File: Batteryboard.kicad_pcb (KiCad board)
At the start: 4 copper layers, 75.8 x 76.2 mm, 143 parts, among them IC1 FAN4010IL6X_F113, IC2 FAN4010IL6X_F113, IC3 FAN4010IL6X_F113, J1 Conn_01x02_Male, J2 Conn_01x03_Male, J4 Conn_01x02_Male, J5 SC_19-20, Q1 SI7617DN-T1-GE3, Q2 SI7617DN-T1-GE3, Q3 SI7617DN-T1-GE3, Q4 SIS412DN-T1-GE3, Q5 SIS412DN-T1-GE3, Q6 SIS412DN-T1-GE3, Q7 SI7617DN-T1-GE3, Q8 SIS412DN-T1-GE3, U1 BQ24617RGET, U2 TPS65279DAPR, U3 BQ29200DRBT, U4 PIC18F25K50-I_SO, U5 MCP2515-xSO, U6 SN65HVD1050D

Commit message: added layout for buck converter
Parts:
- CTTC1: value 43nF -> 47nF
- moved TMP1 64.3 mm to (224.6, 77.6), turned to 270 degrees
- moved R41 39.3 mm to (216.7, 90.6)
- moved R43 34.5 mm to (222.4, 81.9), turned to 180 degrees
- moved C47 33.4 mm to (224.5, 73.1), turned to 270 degrees
- moved C31 30.6 mm to (222.1, 73.0), turned to 270 degrees
- moved C18 30.1 mm to (231.5, 73.0), turned to 270 degrees
- moved IC2 29.0 mm to (216.7, 88.2), turned to 270 degrees
- moved C48 28.5 mm to (226.8, 73.0), turned to 270 degrees
- moved R25 25.1 mm to (237.5, 94.2), turned to 90 degrees
- moved L3 24.6 mm to (242.5, 72.7), turned to 90 degrees
- moved C19 23.1 mm to (231.5, 69.6), turned to 90 degrees
- moved R24 23.1 mm to (233.0, 76.4), turned to 270 degrees
- moved C27 22.7 mm to (248.1, 88.4), turned to 180 degrees
- moved R23 22.3 mm to (231.1, 76.4), turned to 270 degrees
- moved R30 21.8 mm to (237.6, 69.6), turned to 270 degrees
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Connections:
- C1 pad 1: Q5S -> PGND2
- C10 pad 2: Q5S -> PGND2
- C12 pad 2: Q5S -> PGND2
- C13 pad 2: Q5S -> PGND2
- C16 pad 2: Q5S -> PGND2
- C19 pad 2: Q5S -> PGND2
- C2 pad 2: Q5S -> PGND2
- C20 pad 2: Q5S -> PGND2
- C21 pad 2: Q5S -> PGND2
- C22 pad 2: Q5S -> PGND2
- C23 pad 1: Q5S -> PGND2
- C26 pad 1: Q5S -> PGND2
- C27 pad 1: Q5S -> PGND2
- C28 pad 1: Q5S -> PGND2
- C29 pad 1: Q5S -> PGND2
- C31 pad 1: Q5S -> PGND2
- C32 pad 2: Q5S -> PGND2
- C33 pad 1: Q5S -> PGND2
- C34 pad 1: Q5S -> PGND2
- C35 pad 2: Q5S -> PGND2
- C36 pad 2: Q5S -> PGND2
- C37 pad 1: Q5S -> PGND2
- C38 pad 2: Q5S -> PGND2
- C39 pad 1: Q5S -> PGND2
- C4 pad 2: Q5S -> PGND2
- C40 pad 2: Q5S -> PGND2
- C41 pad 1: Q5S -> PGND2
- C42 pad 1: Q5S -> PGND2
- C43 pad 2: Q5S -> PGND2
- C44 pad 1: Q5S -> PGND2
- C45 pad 1: Q5S -> PGND2
- C46 pad 1: Q5S -> PGND2
- C47 pad 1: Q5S -> PGND2
- C48 pad 1: Q5S -> PGND2
- C49 pad 1: Q5S -> PGND2
- C5 pad 2: Q5S -> PGND2
- C7 pad 2: Q5S -> PGND2
- C8 pad 2: Q5S -> PGND2
- C9 pad 2: Q5S -> PGND2
- CCD1 pad 2: Q5S -> PGND2
- CIN2 pad 2: Q5S -> PGND2
- CTTC1 pad 2: Q5S -> PGND2
- CVD1 pad 2: Q5S -> PGND2
- D5 pad 1: Q5S -> PGND2
- IC1 pad 5: Q5S -> PGND2
- IC2 pad 5: Q5S -> PGND2
- IC3 pad 5: Q5S -> PGND2
- J1 pad 2: Q5S -> PGND2
- J2 pad 3: Q5S -> PGND2
- J4 pad 1: Q5S -> PGND2
- J5 pad 1: Q5S -> PGND2
- J5 pad 19: Q5S -> PGND2
- J5 pad 20: Q5S -> PGND2
- J5 pad 36: Q5S -> PGND2
- J5 pad 37: Q5S -> PGND2
- J5 pad 4: Q5S -> PGND2
- J5 pad 40: Q5S -> PGND2
- J5 pad 5: Q5S -> PGND2
- NTCTH1/NTCG163JF103FT1S1 pad 1: Q5S -> PGND2
- Q5 pad 1: Q5S -> PGND2
- Q5 pad 2: Q5S -> PGND2
- Q5 pad 3: Q5S -> PGND2
- Q7 pad 5: Q5S -> PGND2
- Q7 pad 6: Q5S -> PGND2
- Q7 pad 7: Q5S -> PGND2
- Q7 pad 8: Q5S -> PGND2
- Q8 pad 1: Q5S -> PGND2
- Q8 pad 2: Q5S -> PGND2
- Q8 pad 3: Q5S -> PGND2
- R1 pad 2: Q5S -> PGND2
- R10 pad 2: Q5S -> PGND2
- R10/RT1 pad 1: Q5S -> PGND2
- R21 pad 2: Q5S -> PGND2
- R22 pad 2: Q5S -> PGND2
- R25 pad 1: Q5S -> PGND2
- R28 pad 1: Q5S -> PGND2
- R30 pad 1: Q5S -> PGND2
- R36 pad 2: Q5S -> PGND2
- R38 pad 1: Q5S -> PGND2
- R4 pad 2: Q5S -> PGND2
- R41 pad 2: Q5S -> PGND2
- R42 pad 2: Q5S -> PGND2
- R6 pad 2: Q5S -> PGND2
- R8 pad 2: Q5S -> PGND2
- TMP1 pad 3: Q5S -> PGND2
- U1 pad 17: Q5S -> PGND2
- U1 pad 25: Q5S -> PGND2
- U2 pad 10: Q5S -> PGND2
- U2 pad 11: Q5S -> PGND2
- U2 pad 23: Q5S -> PGND2
- U2 pad 3: Q5S -> PGND2
- U2 pad 37: Q5S -> PGND2
- U2 pad 4: Q5S -> PGND2
- U2 pad 9: Q5S -> PGND2
- U3 pad 5: Q5S -> PGND2
- U3 pad 6: Q5S -> PGND2
- U3 pad 9: Q5S -> PGND2
- U4 pad 19: Q5S -> PGND2
- U4 pad 8: Q5S -> PGND2
- U5 pad 18: Q5S -> PGND2
- U6 pad 2: Q5S -> PGND2
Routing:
- net PGND2: track 0.00 -> 140.2 mm, vias 0 -> 48
- net Q5S: track 61.4 -> 0.00 mm, vias 25 -> 1
- net 5V0: track 52.9 -> 85.8 mm, vias 12 -> 19
- net VBAT: track 2.66 -> 28.0 mm, vias 0 -> 4
- net 3V3: track 5.87 -> 20.3 mm
- net FB1: track 0.00 -> 13.7 mm
- net FB2: track 0.00 -> 13.4 mm
- net LX1: track 0.00 -> 12.2 mm
- net Net-(C27-Pad2): track 0.00 -> 11.9 mm
- net Net-(C25-Pad1): track 0.00 -> 11.7 mm
- net Net-(R29-Pad2): track 0.00 -> 10.3 mm
- net Net-(R28-Pad2): track 0.00 -> 9.72 mm
- net Net-(C26-Pad2): track 0.00 -> 9.48 mm
- net Net-(R27-Pad2): track 0.00 -> 9.32 mm
- net RLIM1: track 0.00 -> 7.73 mm
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- added copper zone on B.Cu, net PGND2
- added copper zone on F.Cu, net PGND2
- removed copper zone on B.Cu, net Q5S
- removed copper zone on F.Cu, net Q5S

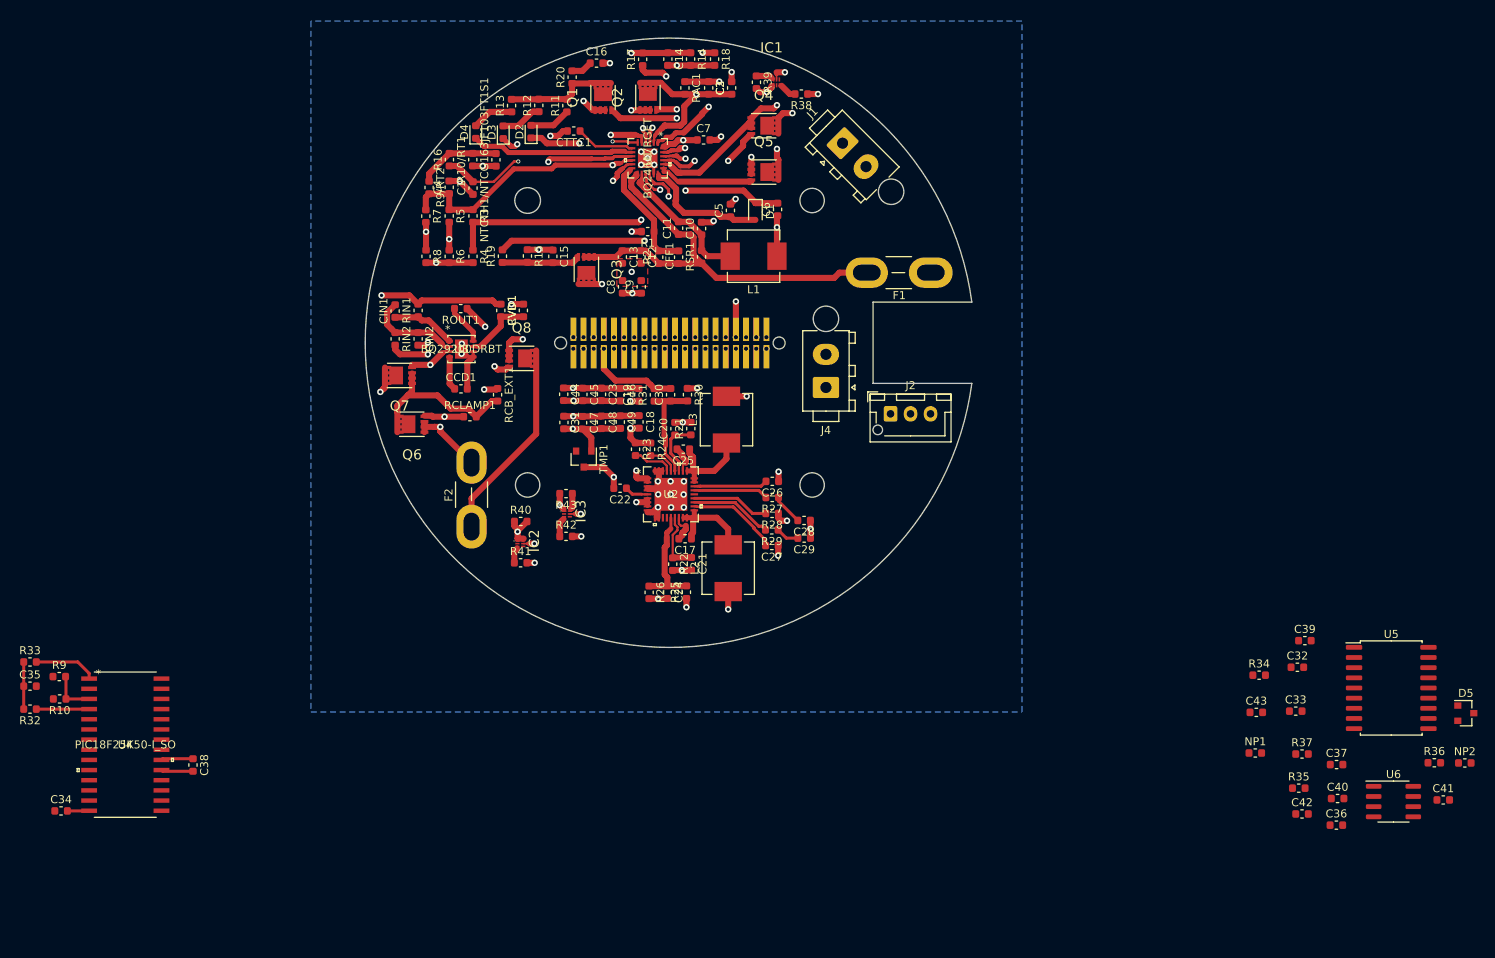
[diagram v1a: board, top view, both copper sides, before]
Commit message: got all components on there, routing and grounding to do still
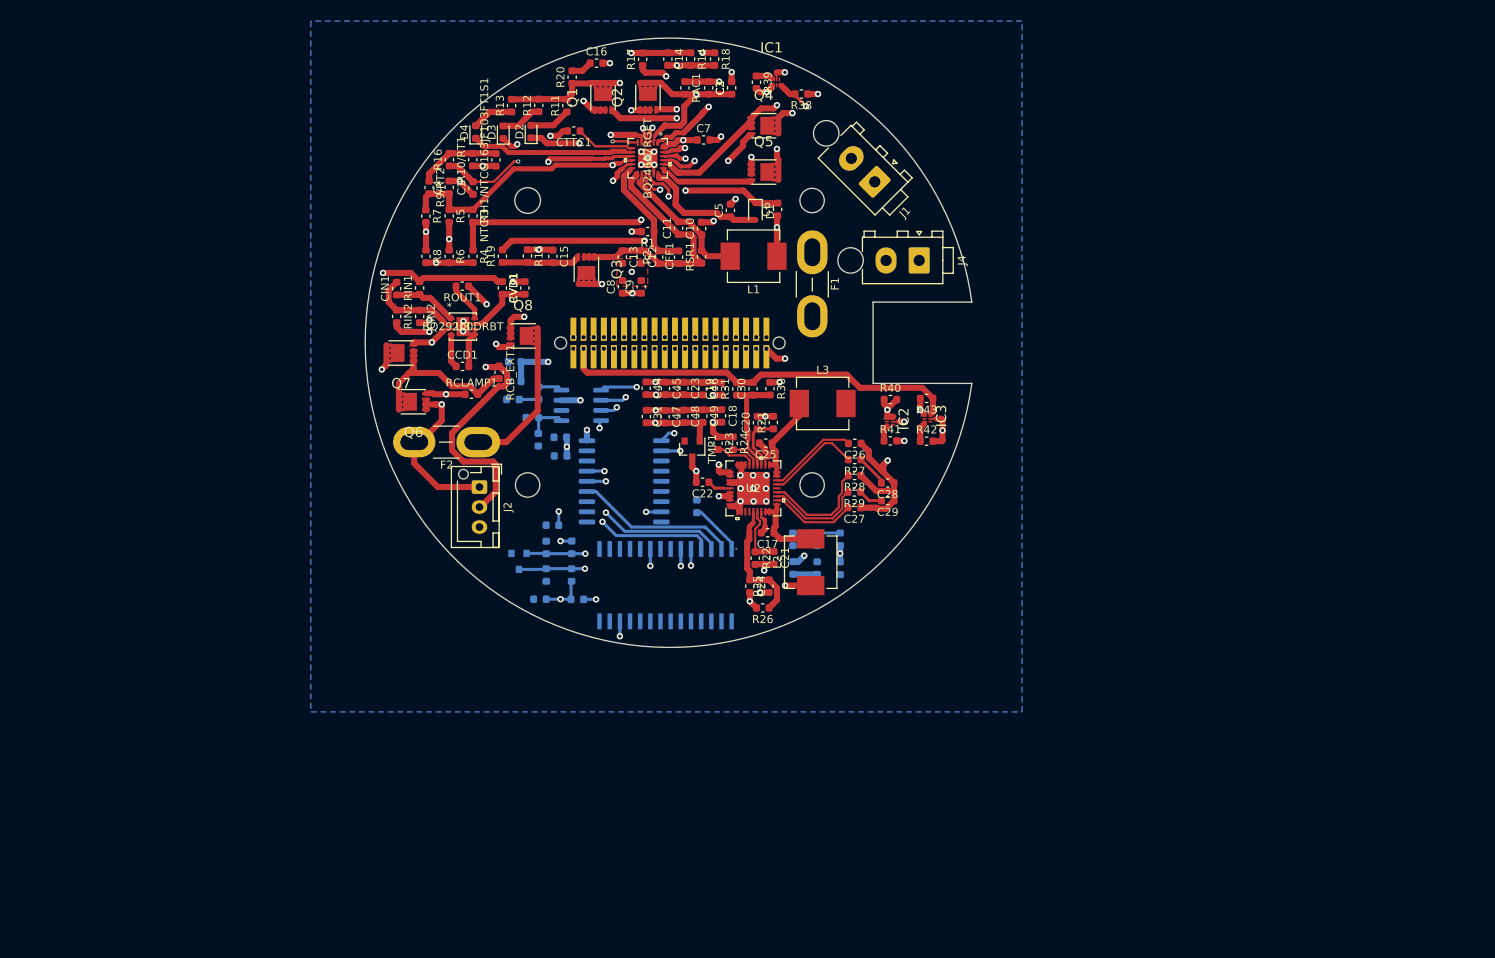
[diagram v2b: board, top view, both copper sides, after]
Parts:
- C32, C33, C34, C35, C36, C37, C38, C39, C40, C41, C42, C43, D5, NP1, NP2, R10, R32, R33, R34, R35, R36, R37, R9, U4, U5, U6: moved to B.Cu
- moved D5 119.9 mm to (216.5, 90.4), turned to 270 degrees
- moved C41 116.5 mm to (219.9, 88.7), turned to 270 degrees
- moved C40 116.5 mm to (216.0, 65.5), turned to 180 degrees
- moved C36 115.9 mm to (215.8, 70.2), turned to 180 degrees
- moved R36 114.2 mm to (220.7, 85.9), turned to 180 degrees
- moved NP2 114.1 mm to (223.1, 92.1), turned to 90 degrees
- moved U6 113.0 mm to (224.3, 70.9)
- moved C37 107.7 mm to (218.9, 75.2), turned to 90 degrees
- moved R35 106.4 mm to (218.2, 72.4), turned to 180 degrees
- moved C39 103.9 mm to (216.0, 67.9)
- moved R32 103.5 mm to (256.7, 87.6), turned to 90 degrees
- moved C35 100.1 mm to (253.8, 87.6), turned to 270 degrees
- moved U5 99.3 mm to (229.7, 80.4)
- moved C42 99.1 mm to (219.9, 92.1), turned to 90 degrees
- moved C33 98.1 mm to (221.7, 74.9)
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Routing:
- net VBATCURRENT: track 2.36 -> 96.1 mm, vias 0 -> 2
- net Net-(J1-Pad1): track 14.1 -> 57.1 mm, vias 0 -> 1
- net 3V3: track 20.3 -> 57.0 mm
- net CAN_L: track 0.00 -> 35.1 mm, vias 0 -> 2
- net Net-(R37-Pad1): track 0.00 -> 34.8 mm, vias 0 -> 2
- net CAN_H: track 0.00 -> 29.5 mm, vias 0 -> 2
- net Net-(J2-Pad2): track 16.5 -> 43.1 mm
- net TX2RTS: track 0.00 -> 24.1 mm, vias 0 -> 2
- net TX1RTS: track 0.00 -> 21.8 mm, vias 0 -> 2
- net SRN: track 53.3 -> 31.6 mm
- net RX1BF: track 0.00 -> 21.1 mm, vias 0 -> 2
- net TX0RTS: track 0.00 -> 20.2 mm
- net RX0BF: track 0.00 -> 19.3 mm, vias 0 -> 2
- net VBAT: track 28.0 -> 45.7 mm, vias 4 -> 5
- net Net-(R36-Pad1): track 0.00 -> 15.5 mm, vias 0 -> 2
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
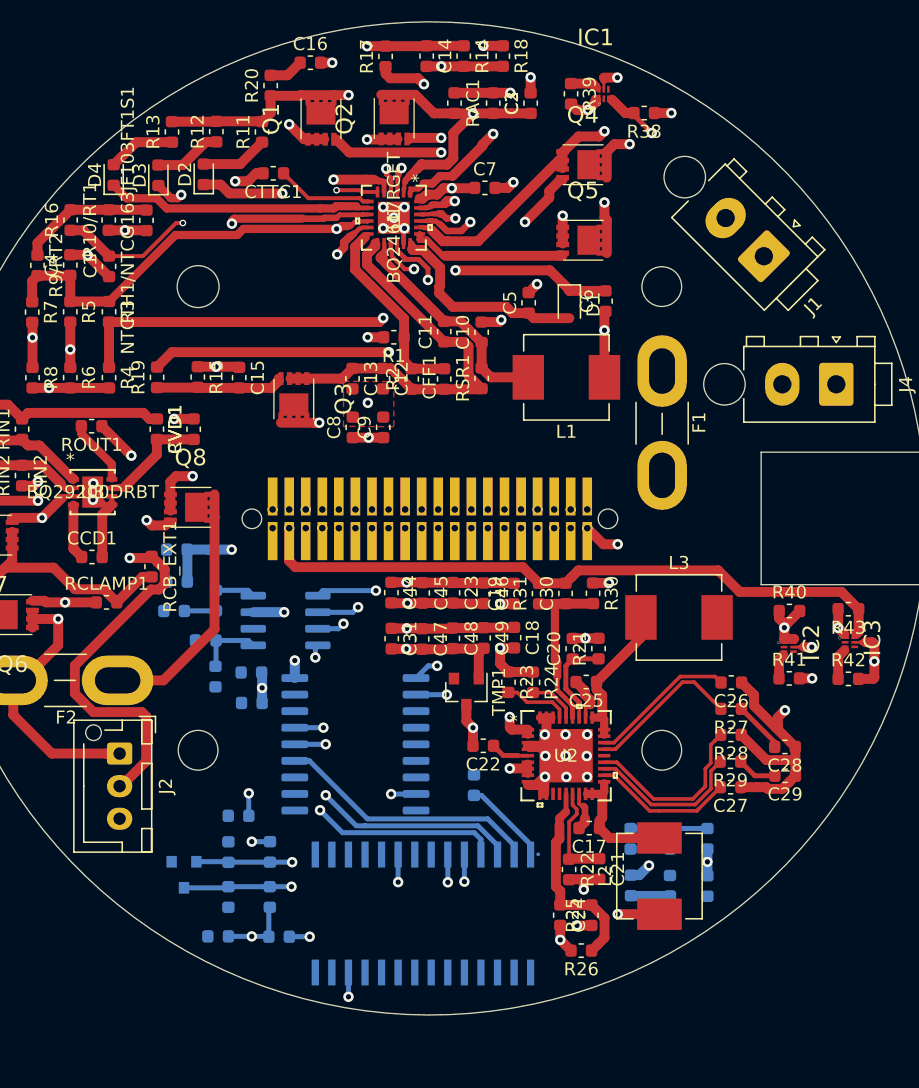
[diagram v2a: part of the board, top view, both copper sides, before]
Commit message: routing done, need to figure out grounding everything still
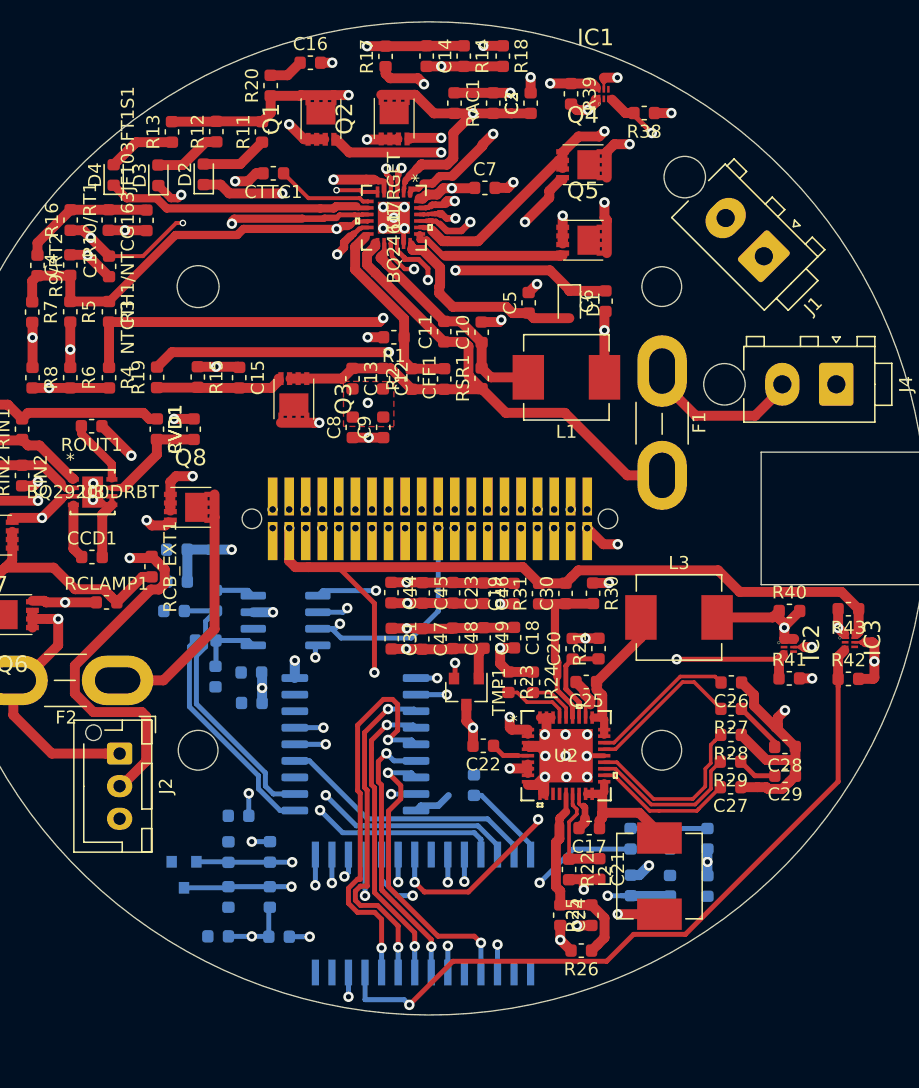
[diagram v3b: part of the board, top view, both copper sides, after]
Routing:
- net TS: track 28.5 -> 115.4 mm, vias 2 -> 4
- net 3V3CURRENT: track 2.66 -> 56.2 mm, vias 0 -> 1
- net VBAT: track 45.7 -> 98.5 mm, vias 5 -> 6
- net 5VCURRENT: track 2.19 -> 44.0 mm, vias 0 -> 3
- net 3V3: track 57.0 -> 92.6 mm, vias 4 -> 6
- net SI: track 0.00 -> 30.7 mm, vias 0 -> 2
- net MCLR: track 0.00 -> 29.9 mm, vias 0 -> 2
- net TEMP_OUT: track 0.00 -> 28.5 mm, vias 0 -> 2
- net Net-(R10-Pad1): track 3.08 -> 30.8 mm, vias 0 -> 2
- net INT: track 0.00 -> 26.1 mm, vias 0 -> 2
- net SCK: track 0.00 -> 23.2 mm, vias 0 -> 2
- net CS: track 0.00 -> 23.0 mm, vias 0 -> 2
- net SO: track 0.00 -> 21.3 mm, vias 0 -> 2
- net Net-(C36-Pad1): track 2.45 -> 21.2 mm
- net Net-(R35-Pad2): track 0.00 -> 17.2 mm
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
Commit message: complete overhaul of board, trying to make it a bit better
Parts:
- added C50: C, Capacitor_SMD:C_0603_1608Metric, F.Cu at (214.9, 86.2)
- added J3: Conn_01x05_Male, Connector_PinHeader_2.54mm:PinHeader_1x05_P2.54mm_Vertical, F.Cu at (211.5, 88.8)
- added R44: R_US, Resistor_SMD:R_0603_1608Metric, F.Cu at (221.2, 90.7)
- added R45: R_US, Resistor_SMD:R_0603_1608Metric, F.Cu at (218.1, 88.5)
- C32, C33, C34, C35, C36, C37, C38, C39, C40, C41, C42, C43, D5, NP1, NP2, R10, R32, R33, R34, R35, R36, R37, R9, U4, U5, U6: moved to F.Cu
- moved F2 61.1 mm to (269.6, 56.7), turned to 270 degrees
- moved J2 59.2 mm to (261.6, 49.3), turned to 0 degrees
- moved R39 51.0 mm to (267.2, 77.0), turned to 90 degrees
- moved IC1 49.3 mm to (265.0, 77.0), turned to 180 degrees
- moved R38 46.4 mm to (263.0, 77.0), turned to 90 degrees
- moved R10 26.4 mm to (228.7, 83.1)
- moved R9 26.1 mm to (226.0, 83.1), turned to 90 degrees
- moved U5 24.0 mm to (207.4, 71.3), turned to 90 degrees
- moved R32 23.4 mm to (233.7, 83.1)
- moved C35 23.0 mm to (231.2, 83.1), turned to 90 degrees
- moved C38 21.9 mm to (236.3, 83.1), turned to 90 degrees
- moved D5 20.3 mm to (222.6, 71.1), turned to 180 degrees
- moved R37 20.1 mm to (220.8, 75.3), turned to 270 degrees
- moved R36 18.3 mm to (222.4, 67.6), turned to 0 degrees
- moved Q8 17.7 mm to (210.3, 45.8), turned to 90 degrees
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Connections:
- C15 pad 1: 5V0 -> Q4D
- C23 pad 2: 5V0 -> Net-(C23-Pad2)
- C3 pad 1: 5V0 -> Q4D
- C31 pad 2: 5V0 -> Net-(C31-Pad2)
- C44 pad 2: 5V0 -> Net-(C23-Pad2)
- C45 pad 2: 5V0 -> Net-(C23-Pad2)
- C46 pad 2: 5V0 -> Net-(C23-Pad2)
- C47 pad 2: 5V0 -> Net-(C31-Pad2)
- C48 pad 2: 5V0 -> Net-(C31-Pad2)
- C49 pad 2: 5V0 -> Net-(C31-Pad2)
- C8 pad 1: 5V0 -> Q4D
- C9 pad 1: 5V0 -> Q4D
- IC1 pad 1: 5V0 -> Q4D
- IC2 pad 1: 5V0 -> Net-(C23-Pad2)
- IC3 pad 1: 5V0 -> Net-(C31-Pad2)
- L2 pad 1: 5V0 -> Net-(C23-Pad2)
- L3 pad 2: 5V0 -> Net-(C31-Pad2)
- Q3 pad 5: 5V0 -> Q4D
- Q3 pad 6: 5V0 -> Q4D
- Q3 pad 7: 5V0 -> Q4D
- Q3 pad 8: 5V0 -> Q4D
- Q4 pad 5: 5V0 -> Q4D
- Q4 pad 6: 5V0 -> Q4D
- Q4 pad 7: 5V0 -> Q4D
- Q4 pad 8: 5V0 -> Q4D
- R15 pad 1: 5V0 -> Q4D
- R39 pad 2: 5V0 -> Q4D
- R40 pad 1: 5V0 -> Net-(C23-Pad2)
- R43 pad 2: 5V0 -> Net-(C31-Pad2)
- RAC1 pad 1: 5V0 -> Q4D
- U1 pad 1: 5V0 -> Q4D
- U4 pad 27: Net-(U4-Pad27) -> PGC
- U4 pad 28: Net-(U4-Pad28) -> PGD
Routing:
- net TS: track 115.4 -> 2.56 mm, vias 4 -> 0
- net VBATCURRENT: track 96.1 -> 2.43 mm, vias 2 -> 0
- net VBAT: track 98.5 -> 10.3 mm, vias 6 -> 0
- net 3V3: track 92.6 -> 8.80 mm, vias 6 -> 0
- net 5V0: track 94.7 -> 19.5 mm, vias 25 -> 7
- net 3V3CURRENT: track 56.2 -> 2.45 mm, vias 1 -> 0
- net PGND2: track 157.1 -> 112.7 mm, vias 45 -> 59
- net Net-(J1-Pad1): track 57.1 -> 14.1 mm, vias 1 -> 0
- net 5VCURRENT: track 44.0 -> 2.44 mm, vias 3 -> 0
- net CAN_L: track 46.2 -> 5.47 mm, vias 3 -> 0
- net Q6S: track 56.9 -> 17.4 mm
- net CAN_H: track 46.1 -> 7.55 mm, vias 3 -> 0
- net Net-(C31-Pad2): track 0.00 -> 37.5 mm, vias 0 -> 3
- net Net-(C23-Pad2): track 0.00 -> 36.7 mm
- net ISET2: track 36.3 -> 0.00 mm, vias 2 -> 0
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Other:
- board size 75.8 x 76.2 mm -> 76.2 x 76.2 mm

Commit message: finished for the night, 80 something traces left, then onto implementing proper grounding, which should be easy given that I have a huge uninterrupted ground plane to work with
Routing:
- net Q4D: track 25.0 -> 69.5 mm, vias 0 -> 2
- net ACSET: track 0.00 -> 34.4 mm, vias 0 -> 2
- net Net-(C23-Pad2): track 36.7 -> 70.3 mm, vias 0 -> 2
- net VBAT: track 10.3 -> 43.2 mm, vias 0 -> 4
- net ISET2: track 0.00 -> 30.1 mm, vias 0 -> 2
- net Q4S: track 15.9 -> 40.2 mm, vias 0 -> 4
- net Net-(R7-Pad2): track 2.91 -> 25.0 mm, vias 0 -> 2
- net Net-(R19-Pad2): track 0.00 -> 19.5 mm, vias 0 -> 2
- net Net-(C14-Pad2): track 7.99 -> 25.6 mm, vias 0 -> 3
- net BTST: track 2.77 -> 19.0 mm, vias 0 -> 2
- net Q4G: track 0.00 -> 13.7 mm, vias 0 -> 2
- net Q6S: track 17.4 -> 29.8 mm, vias 2 -> 4
- net VFB: track 5.46 -> 17.4 mm, vias 0 -> 2
- net FB1: track 6.44 -> 17.3 mm
- net RLIM1: track 2.34 -> 13.0 mm
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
